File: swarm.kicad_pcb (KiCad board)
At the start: 2 copper layers, 60 x 30 mm, 29 parts, among them P1 USB_OTG, P2 CONN_01X05, P3 CONN_02X20, SW1 SW_PUSH, U1 LM3671MF-3.3, U2 STM32F103RETx, U3 APA102, Y1 Crystal

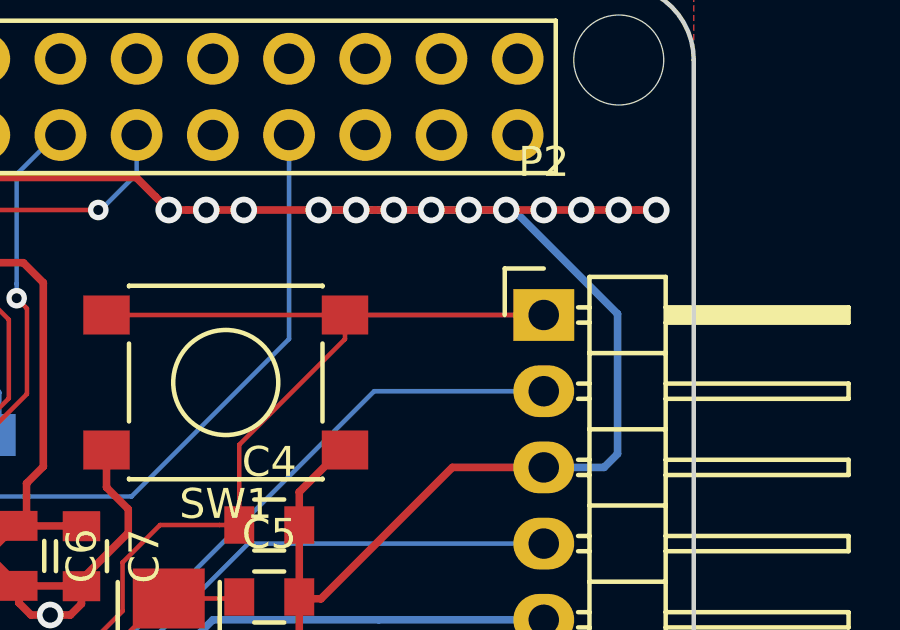
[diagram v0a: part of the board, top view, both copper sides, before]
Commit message: Removes unnecessary track on bottom (NRST)
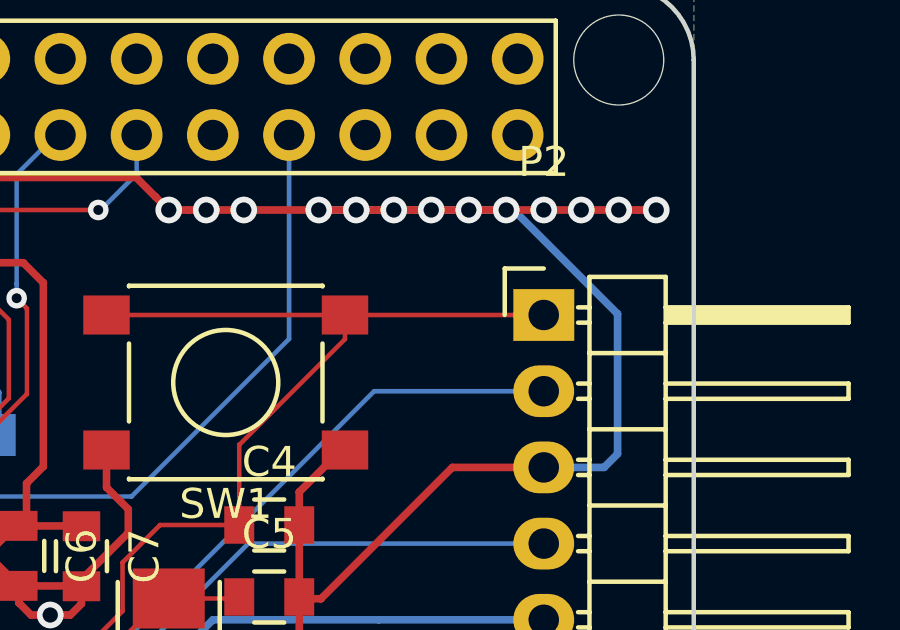
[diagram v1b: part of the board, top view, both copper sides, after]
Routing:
- net /NRST: track 40.9 -> 34.6 mm
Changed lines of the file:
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@@
     (links 102)
     (no_connects 0)
-    (area 95.069814 67.5091 165.890901 104.540901)
+    (area 99.924999 69.924999 160.075001 100.075001)
     (thickness 1.6002)
     (drawings 8)
-    (tracks 733)
+    (tracks 732)
     (zones 0)
     (modules 29)
@@
   (segment (start 144.85 87.1526) (end 144.85 87.93) (width 0.1524) (layer Top) (net 36))
   (segment (start 155 81) (end 148.375 81) (width 0.1524) (layer Top) (net 36))
-  (segment (start 148.75 81) (end 155 81) (width 0.1524) (layer Bottom) (net 36))
   (segment (start 132.942022 93.151501) (end 132.478231 93.615294) (width 0.1524) (layer Bottom) (net 37))
   (segment (start 131.929587 93.615294) (end 131.905803 93.59151) (width 0.1524) (layer Bottom) (net 37))

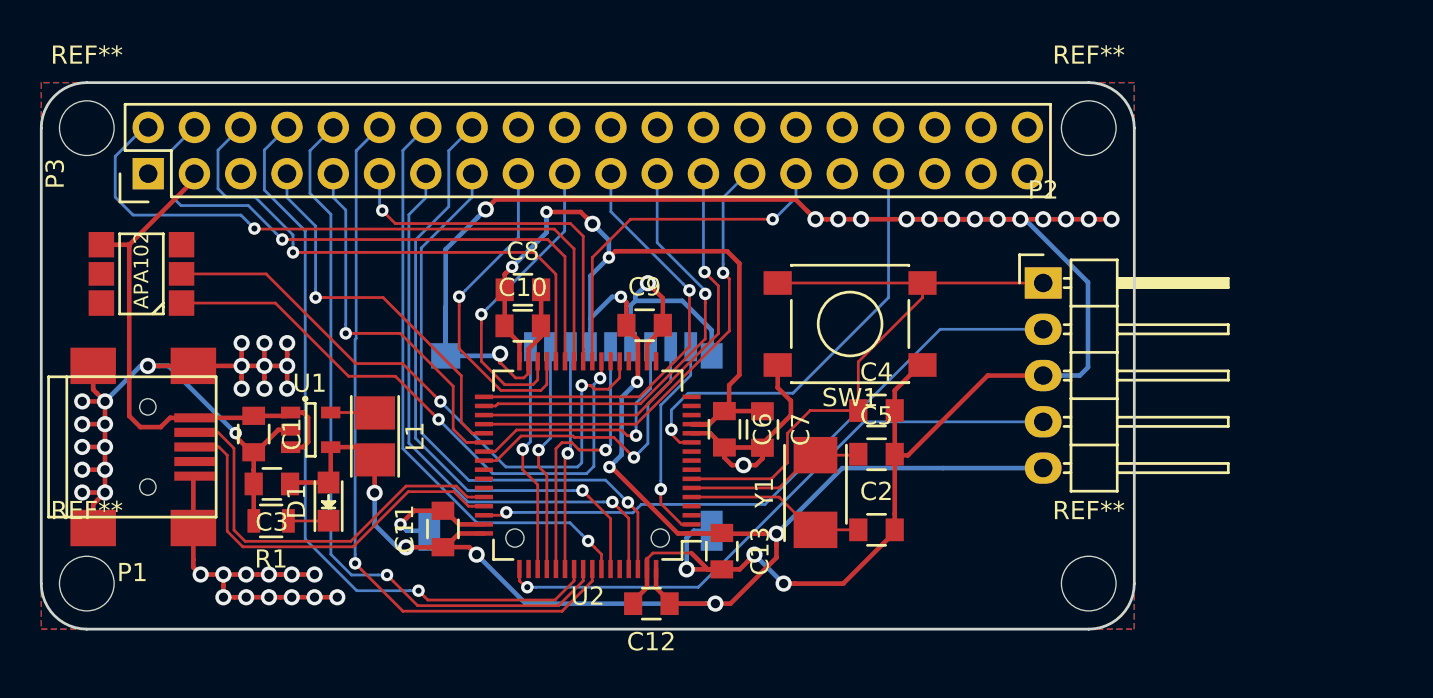
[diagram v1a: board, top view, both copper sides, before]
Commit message: Adds fuse (MF-PSMF050X) to schematic and layout
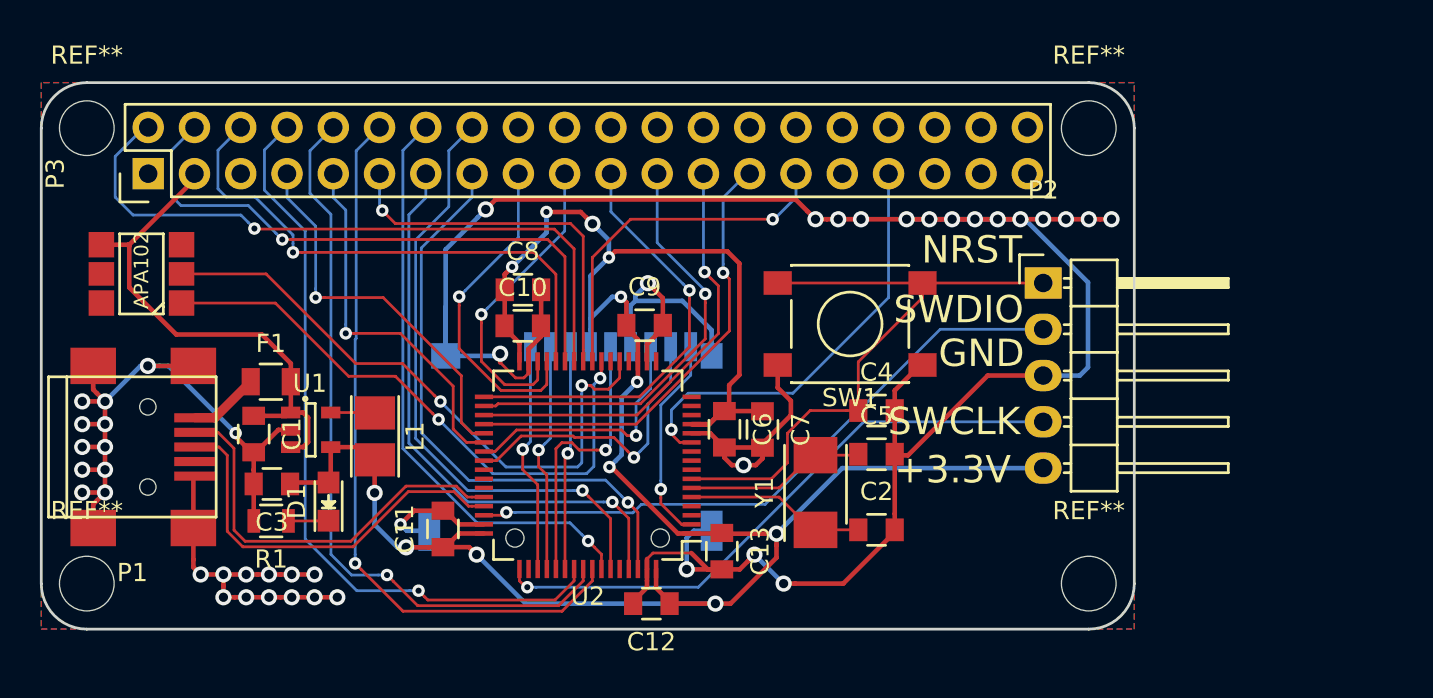
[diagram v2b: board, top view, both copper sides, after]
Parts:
- added F1: FUSE, volium:MF-PSMF050X, F.Cu at (112.6, 86.4)
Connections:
- P1 pad 1: VCC -> Net-(F1-Pad1)
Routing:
- net GND: track 223.9 -> 211.2 mm, vias 54 -> 45
- net Net-(F1-Pad1): track 0.00 -> 3.87 mm
- net VCC: track 29.7 -> 28.7 mm
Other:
- net class Fuse added: clearance 0.2159, trace_width 0.508, via_dia 0.6858, via_drill 0.3302
- board text added: "+3.3V"
- board text added: "GND"
- board text added: "NRST"
- board text added: "SWCLK"
- board text added: "SWDIO"

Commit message: Updates footprints, adds via to connect ground to APA102
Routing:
- net GND: track 211.2 -> 224.1 mm, vias 45 -> 46

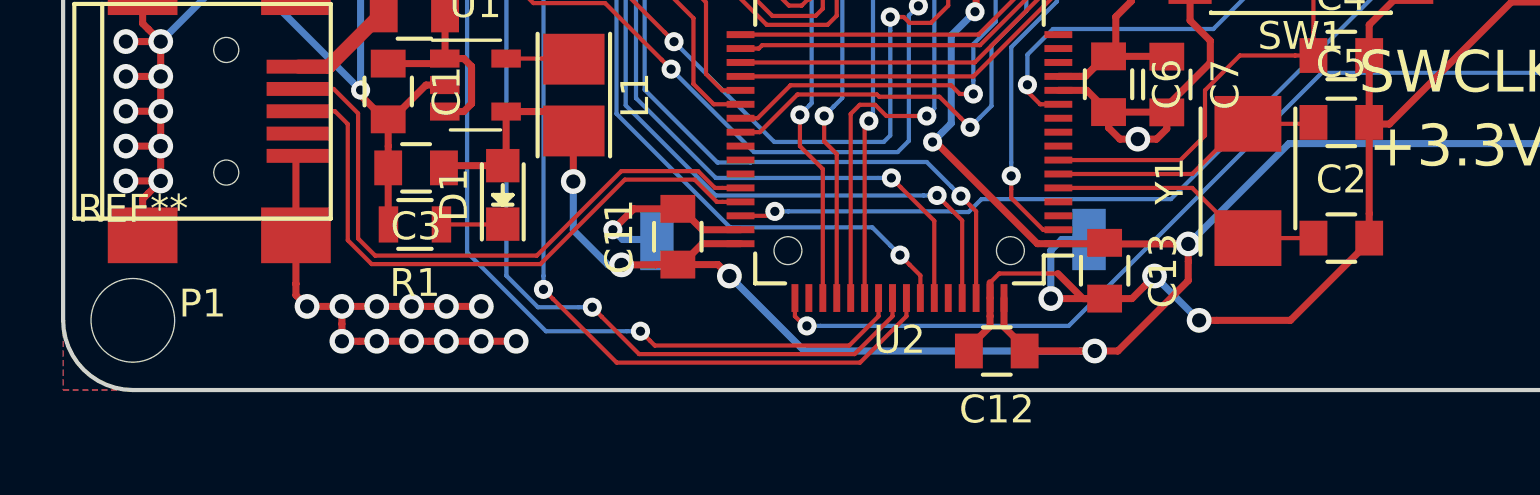
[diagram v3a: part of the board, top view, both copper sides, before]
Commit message: Via stitching
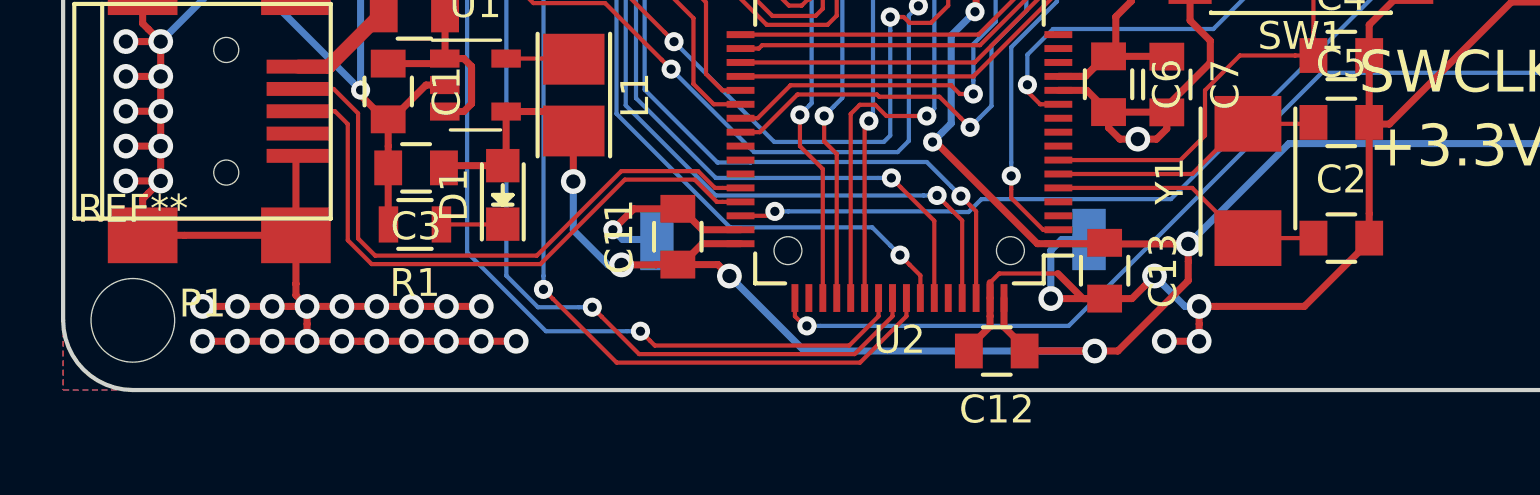
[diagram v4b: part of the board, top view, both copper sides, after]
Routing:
- net GND: track 224.1 -> 240.4 mm, vias 46 -> 55

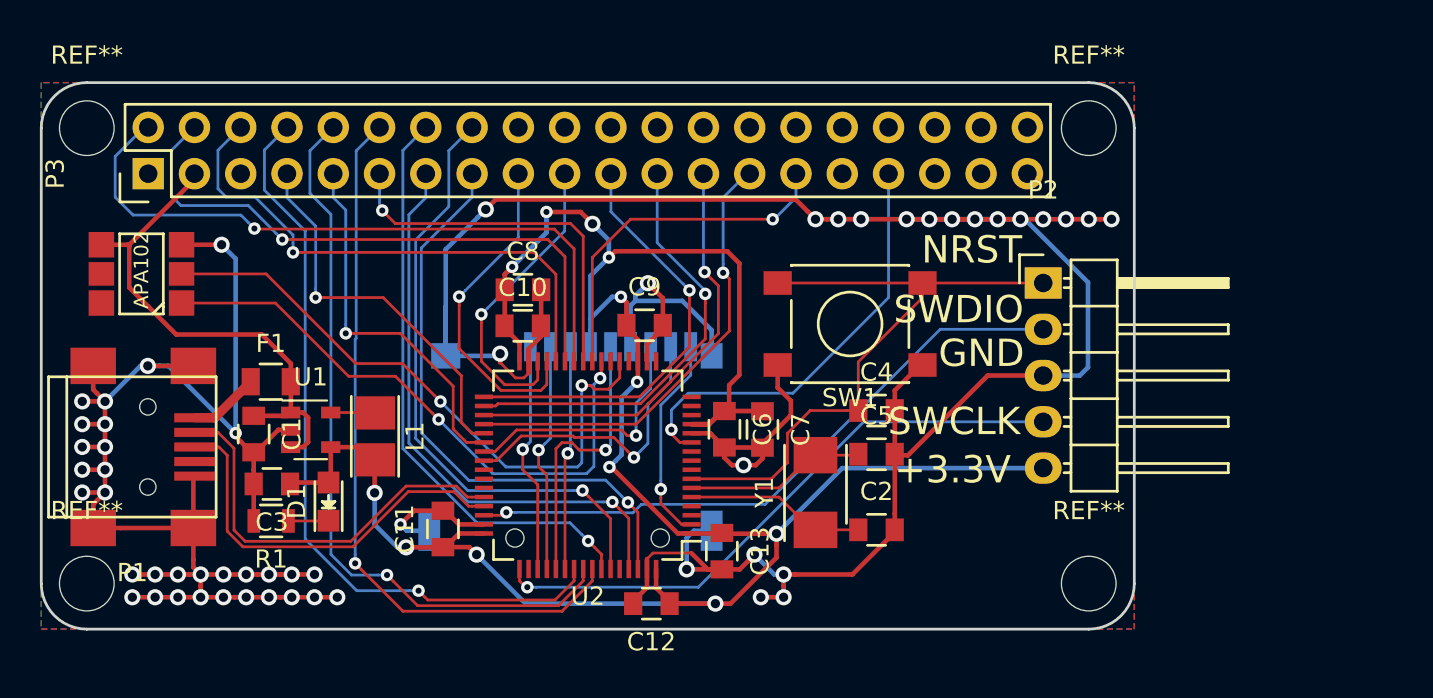
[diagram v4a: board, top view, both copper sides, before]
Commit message: Fixes pinout of debug connector, still needs to reroute
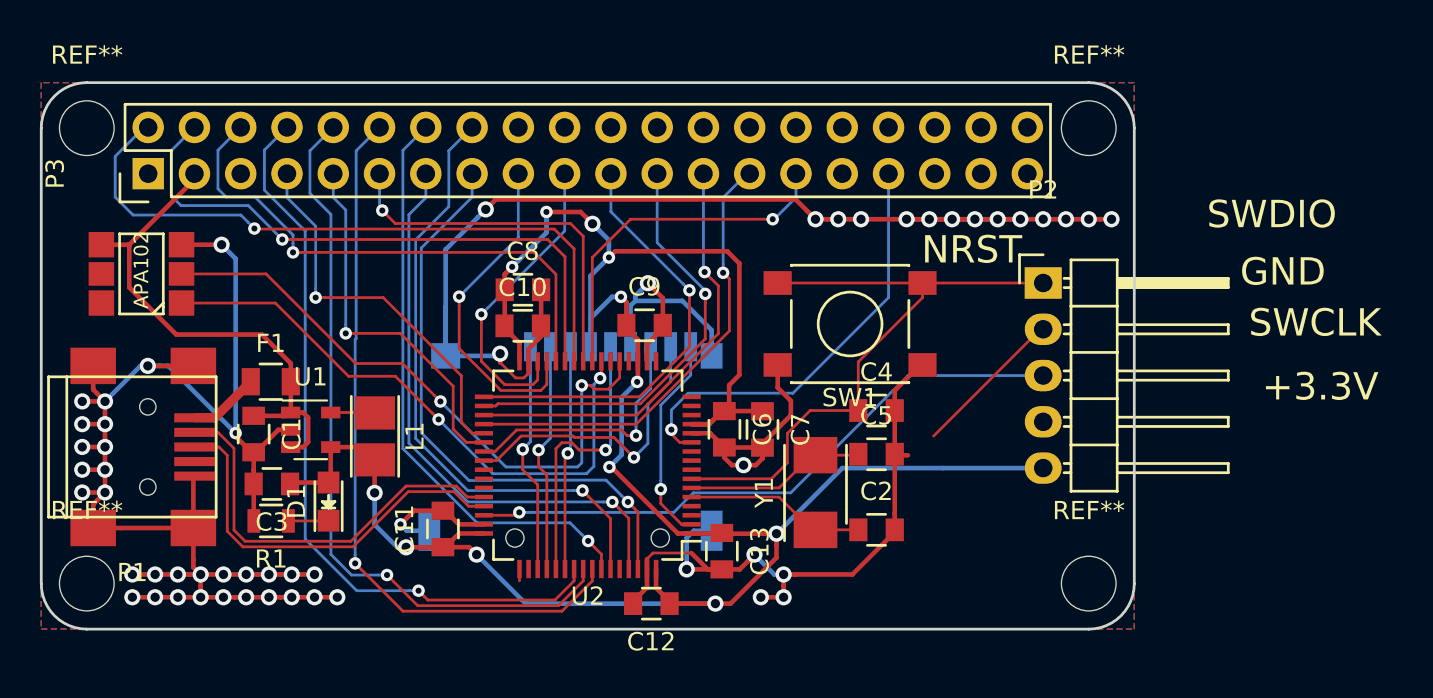
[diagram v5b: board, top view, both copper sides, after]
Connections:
- P2 pad 2: /SWDIO -> /SWCLK
- P2 pad 3: GND -> /SWDIO
- P2 pad 4: /SWCLK -> GND
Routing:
- net /SWCLK: track 33.3 -> 9.10 mm, vias 1 -> 0
- net GND: track 240.4 -> 219.0 mm
- net /SWDIO: track 34.9 -> 33.9 mm

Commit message: More changes Finished routing debug connector Added labels to debug connector pins
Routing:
- net /SWCLK: track 9.10 -> 47.0 mm, vias 0 -> 1
- net /LCD_D2: track 29.7 -> 29.1 mm
- net +3V3: track 125.3 -> 124.7 mm

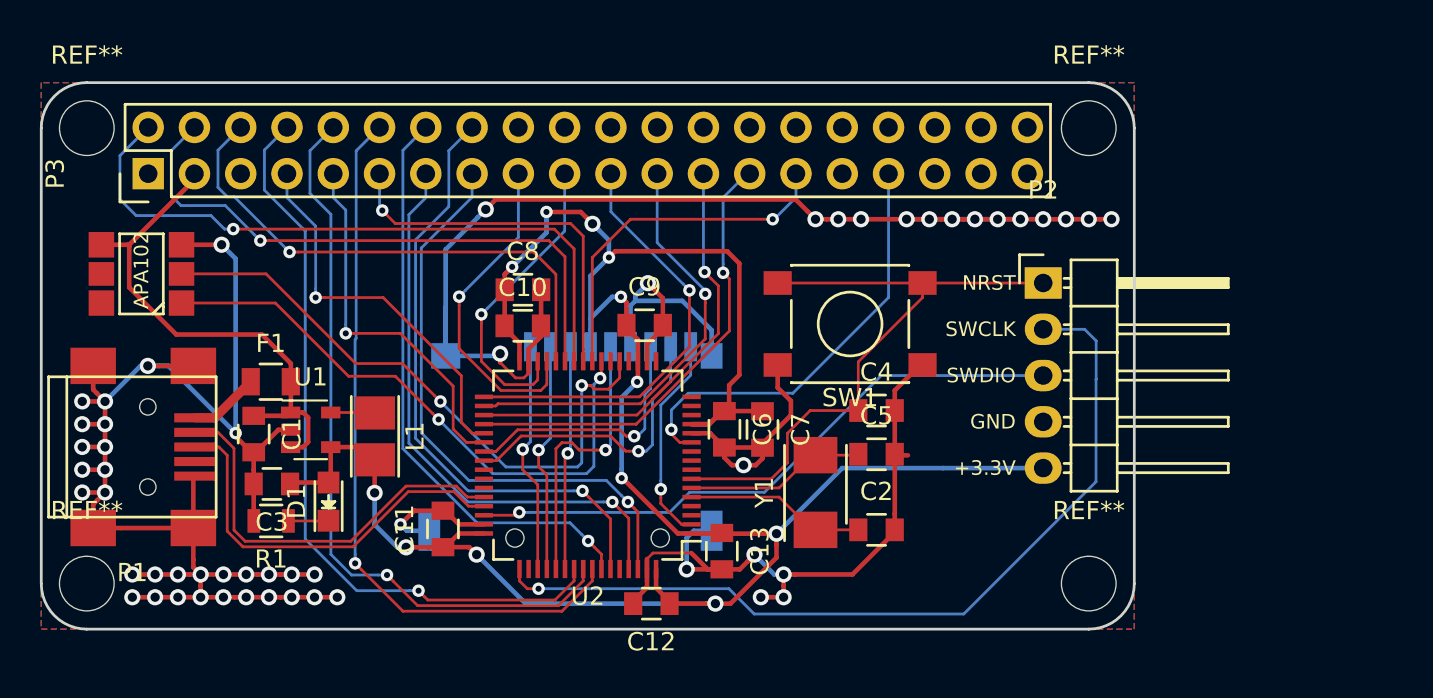
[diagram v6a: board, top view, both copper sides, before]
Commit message: Cleanup Added back 3D model for L1 inductor (lost in a previous commit) More via stitching
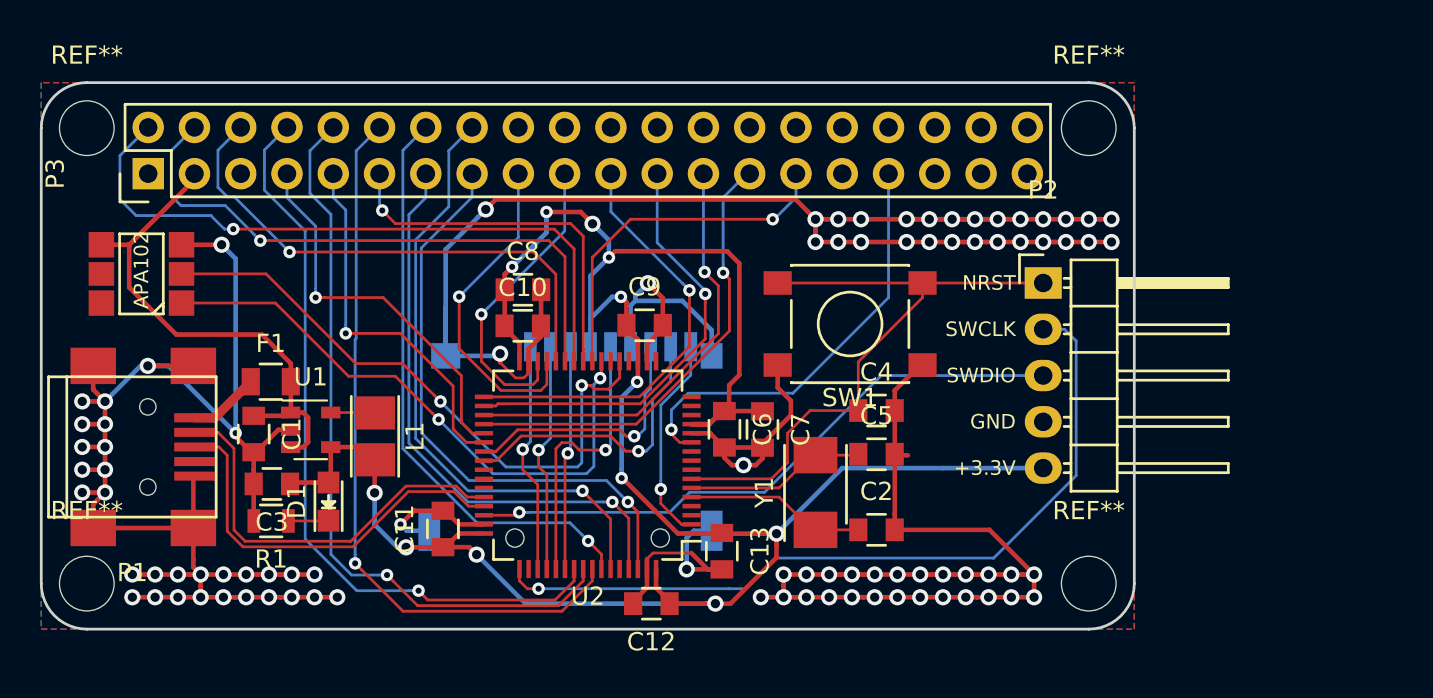
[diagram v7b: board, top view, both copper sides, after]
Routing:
- net GND: track 219.0 -> 262.7 mm, vias 55 -> 89
- net /SWCLK: track 47.0 -> 43.4 mm

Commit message: More cleanup Moved some tracks, reran DRC
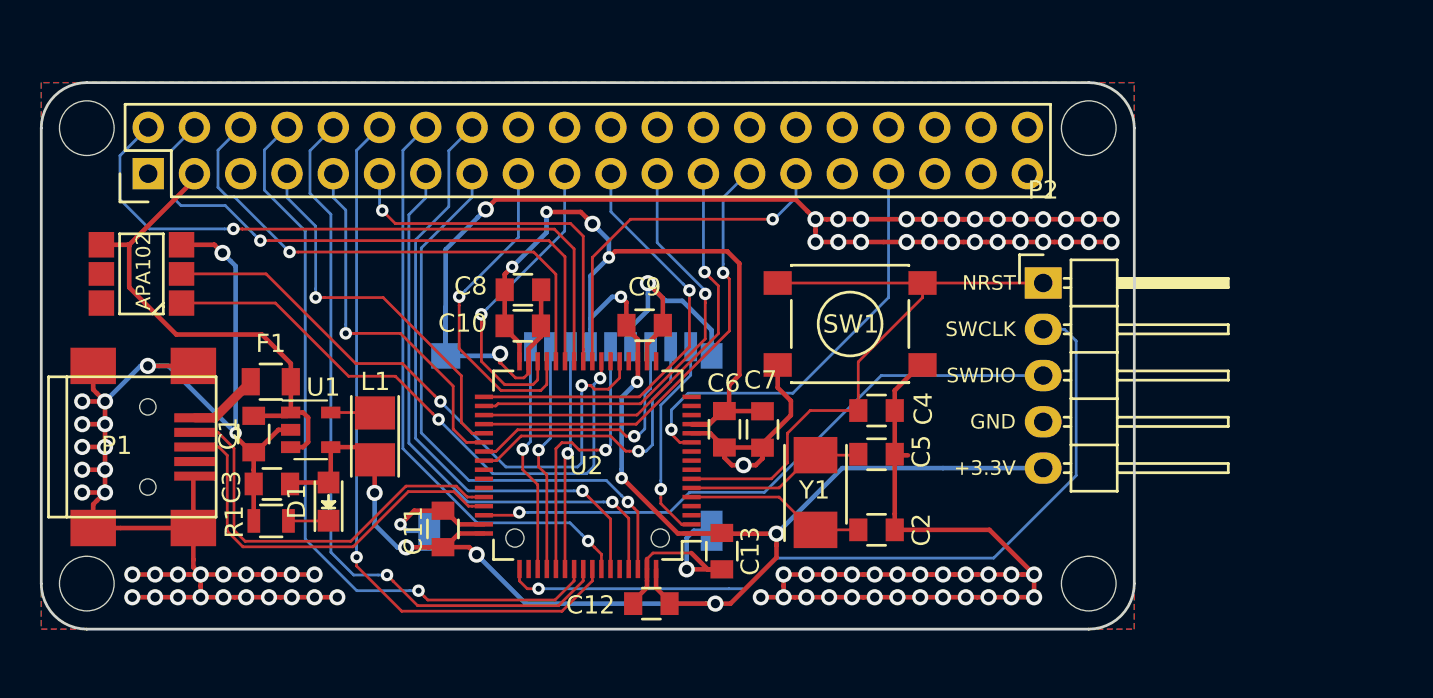
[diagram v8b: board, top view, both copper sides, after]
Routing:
- net GND: track 262.7 -> 262.1 mm
